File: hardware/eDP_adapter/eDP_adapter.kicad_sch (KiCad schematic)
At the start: 90 parts, among them J1 DF12NB(3.0)-30DS-0.5V(51), J2 DF12NB(3.0)-30DS-0.5V(51), J3 Conn_01x40, J4 Barrel_Jack_MountingPin, Q1 2N7002WT1G, U1 NCS8801, U2 EA3036A, U3 MT3608

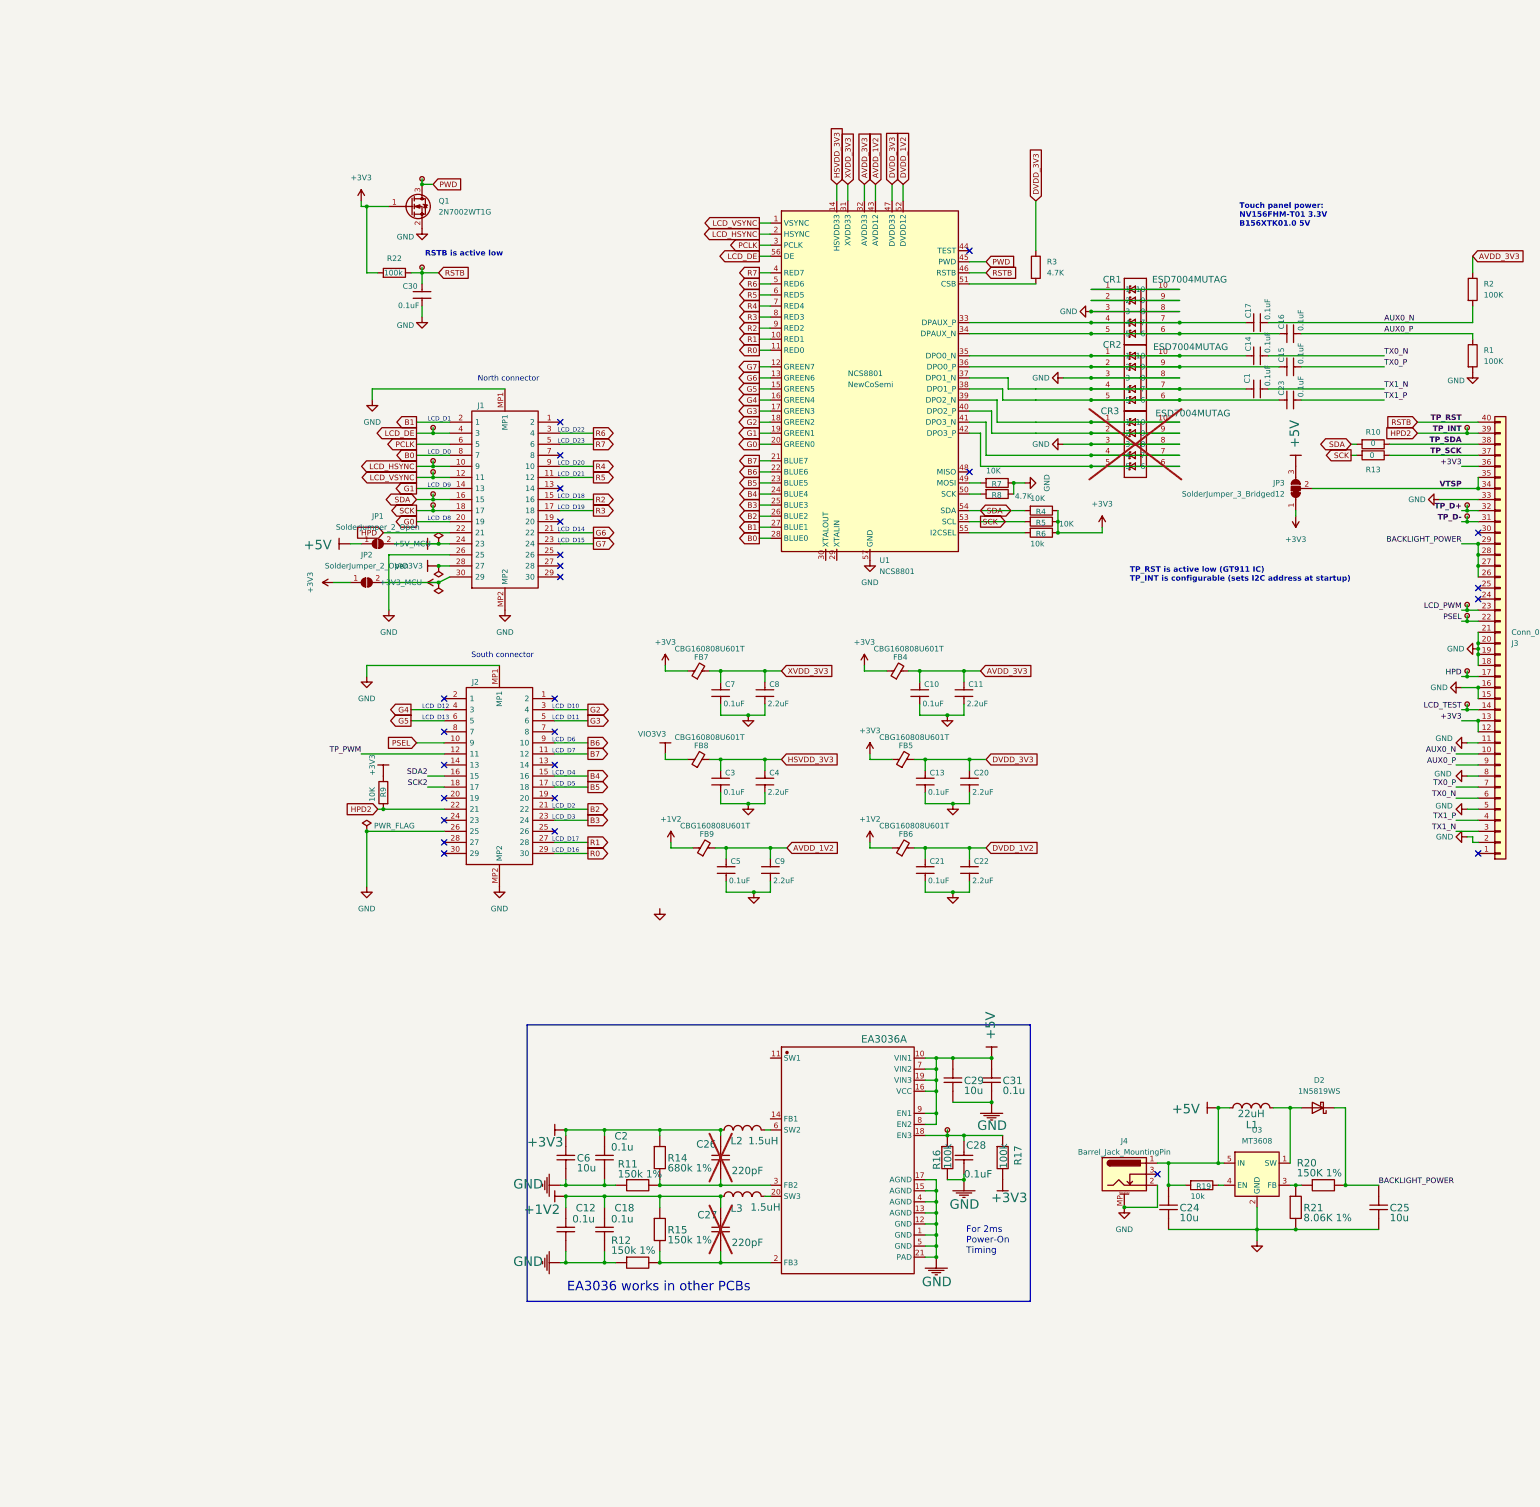
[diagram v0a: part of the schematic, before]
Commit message: make eDP adaoter 4 layer and misc fixes (like missing crystal)
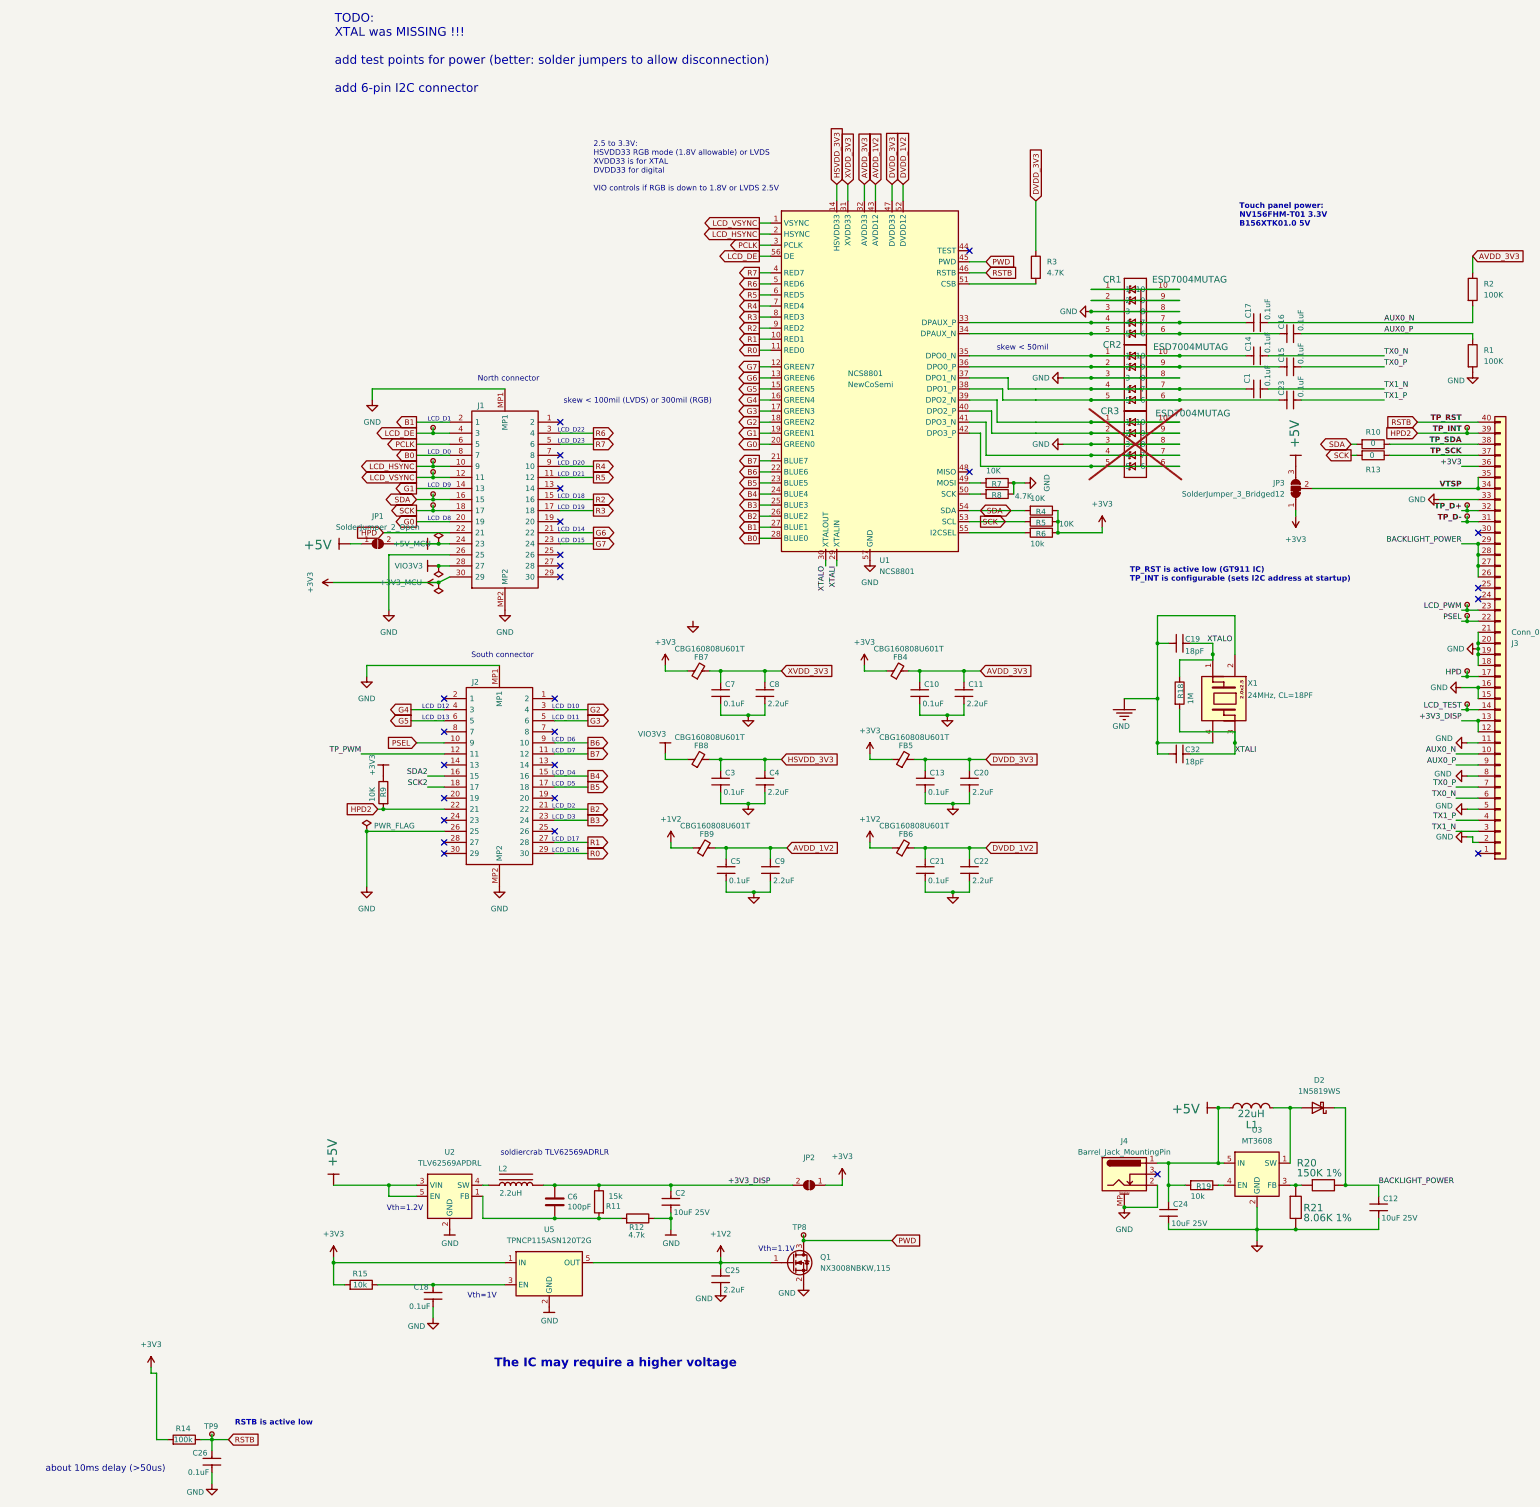
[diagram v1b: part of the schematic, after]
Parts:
- removed C12, C18, C2: 0.1u, Capacitor_SMD:C_0603_1608Metric, symbol C_0402_US_4
- removed C24, C25, C29, C6: 10u, Capacitor_SMD:C_0603_1608Metric, symbol C_0402_US_7
- removed C26, C27: 220pF, Capacitor_SMD:C_0603_1608Metric, symbol C_0402_US_4
- removed C28: 0.1uF, Capacitor_SMD:C_0402_1005Metric, symbol GRM188B30J106ME47D_14
- removed C30: 0.1uF, Library:C_0402_1005Metric, symbol Periph-altium-import:0_CAP
- removed C31: 0.1u, Capacitor_SMD:C_0603_1608Metric, symbol C_0402_US_6
- removed L2: 1.5uH, Inductor_SMD:L_Cenker_CKCS201610, symbol CKCS201610-2.2UH/M-N_1
- removed L3: 1.5uH, Inductor_SMD:L_Cenker_CKCS201610, symbol CKCS201610-2.2UH/M-N
- removed R11: 150k 1%, Resistor_SMD:R_0402_1005Metric, symbol R_0402_EU_2
- removed R12: 150k 1%, Resistor_SMD:R_0402_1005Metric, symbol R_0402_EU
- removed R14: 680k 1%, Resistor_SMD:R_0402_1005Metric, symbol R_0402_EU_3
- removed R15: 150k 1%, Resistor_SMD:R_0402_1005Metric, symbol R_0402_EU_1
- removed R16: 100k, Resistor_SMD:R_0402_1005Metric, symbol R_0603_EU_1
- removed R17: 100k, Resistor_SMD:R_0402_1005Metric, symbol R_0603_EU
- removed R22: 100k, Resistor_SMD:R_0402_1005Metric, symbol Device:R
- removed TP10, TP11: TestPoint_Small, TestPoint:TestPoint_Pad_D1.0mm, symbol Connector:TestPoint_Small
- removed U2: EA3036A, Package_DFN_QFN:WQFN-20-1EP_3x3mm_P0.4mm_EP1.7x1.7mm, symbol EA3036A
- added C12, C2, C24: 10uF 25V, Capacitor_SMD:C_0805_2012Metric, symbol Periph-altium-import:0_CAP
- added C18, C26: 0.1uF, Library:C_0402_1005Metric, symbol Periph-altium-import:0_CAP
- added C19, C32: 18pF, Library:C_0402_1005Metric, symbol D1s-altium-import:1_mirrored_CAP
- added C25: 2.2uF, Library:C_0402_1005Metric, symbol Periph-altium-import:0_CAP
- added C6: 100pF, Capacitor_SMD:C_0201_0603Metric, symbol Device:C
- added L2: 2.2uH, Library:Murata_DFE201612P-2R2M=P2, symbol Periph-altium-import:0_L
- added R11: 15k, Resistor_SMD:R_0201_0603Metric, symbol Device:R
- added R12: 4.7k, Resistor_SMD:R_0201_0603Metric, symbol Device:R
- added R14: 100k, Resistor_SMD:R_0402_1005Metric, symbol Device:R
- added R15: 10k, Resistor_SMD:R_0402_1005Metric, symbol Device:R
- added R18: 1M, Resistor_SMD:R_0402_1005Metric, symbol Device:R
- added TP8: TestPoint_Small, TestPoint:TestPoint_Pad_D1.0mm, symbol Connector:TestPoint_Small
- added U2: TLV62569APDRL, Package_TO_SOT_SMD:SOT-563, symbol Regulator_Switching:TLV62569DRL
- added U5: TPNCP115ASN120T2G, Package_TO_SOT_SMD:SOT-23-5, symbol Regulator_Linear:NCP115AMX250TCG
- added X1: 24MHz, CL=18PF, Library:Crystal_SMD_2520-4Pin_2.5x2.0mm, symbol D1s-altium-import:3_mirrored_XTAL3225
- Q1: value 2N7002WT1G -> NX3008NBKW,115; MPN 2N7002WT1G -> NX3008NBKW,115
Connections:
- net +1V2: now also Q1.1 (G), C25.1, U5.5 (OUT)
- net +3V3: now also J1.30 (29), R14.2, R15.2, U5.1 (IN); no longer J3.12 (Pin_12), J3.13 (Pin_13), Q1.1 (G)
- net +5V: now also C24.1, U2.3 (VIN), U2.5 (EN)
- net BACKLIGHT_POWER: now also C12.1
- net GND: now also C12.2, C18.2, C19.2, C2.2, C24.2, C25.2, C26.2, C32.2, R12.1, U2.2 (GND), U5.2 (GND), U5.5 (OUT), X1.2 (NC1), X1.4 (NC2)
- net PWD: now also TP8.1
- net RSTB: now also C26.1, R14.1
- net XTALI: now reaches U1.29 (XTALIN)
- net XTALI: now also C32.1, R18.2, X1.3 (X2)
- net XTALO: now reaches U1.30 (XTALOUT)
- net XTALO: now also C19.1, R18.1, X1.1 (X1)
- net +3V3_MCU renamed +3V3_DISP
- net +3V3_DISP: now also J3.12 (Pin_12), J3.13 (Pin_13), C2.1, C6.2, L2.1, R11.1; no longer J1.30 (29)
- new net: C6.1, R11.2, R12.2, U2.1 (FB)
- new net: L2.2, U2.4 (SW)
- new net: C18.1, R15.1, U5.3 (EN)
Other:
- note added: "2.5 to 3.3V: HSVDD33 RGB mode (1.8V allowable) or LVDS XVDD33 is for XTAL DVDD33 for digital VIO controls if RGB is down to 1.8V or LVDS 2.5V"
- note added: "TODO: XTAL was MISSING !!! add test points for power (better: solder jumpers to allow disconnection) add 6-pin I2C connector"
- note added: "The IC may require a higher voltage"
- note added: "Vth=1.1V"
- note added: "Vth=1.2V"
- note added: "Vth=1V"
- note added: "about 10ms delay (>50us)"
- note added: "skew < 100mil (LVDS) or 300mil (RGB)"
- note added: "skew < 50mil"
- note added: "soldiercrab TLV62569ADRLR"
- note removed: "EA3036 works in other PCBs"
- note removed: "For 2ms Power-On Timing"
- company: Copyright (C) 2025 Victor Suarez Rovere -> Copyright (C) 2025-2026 Victor Suarez Rovere

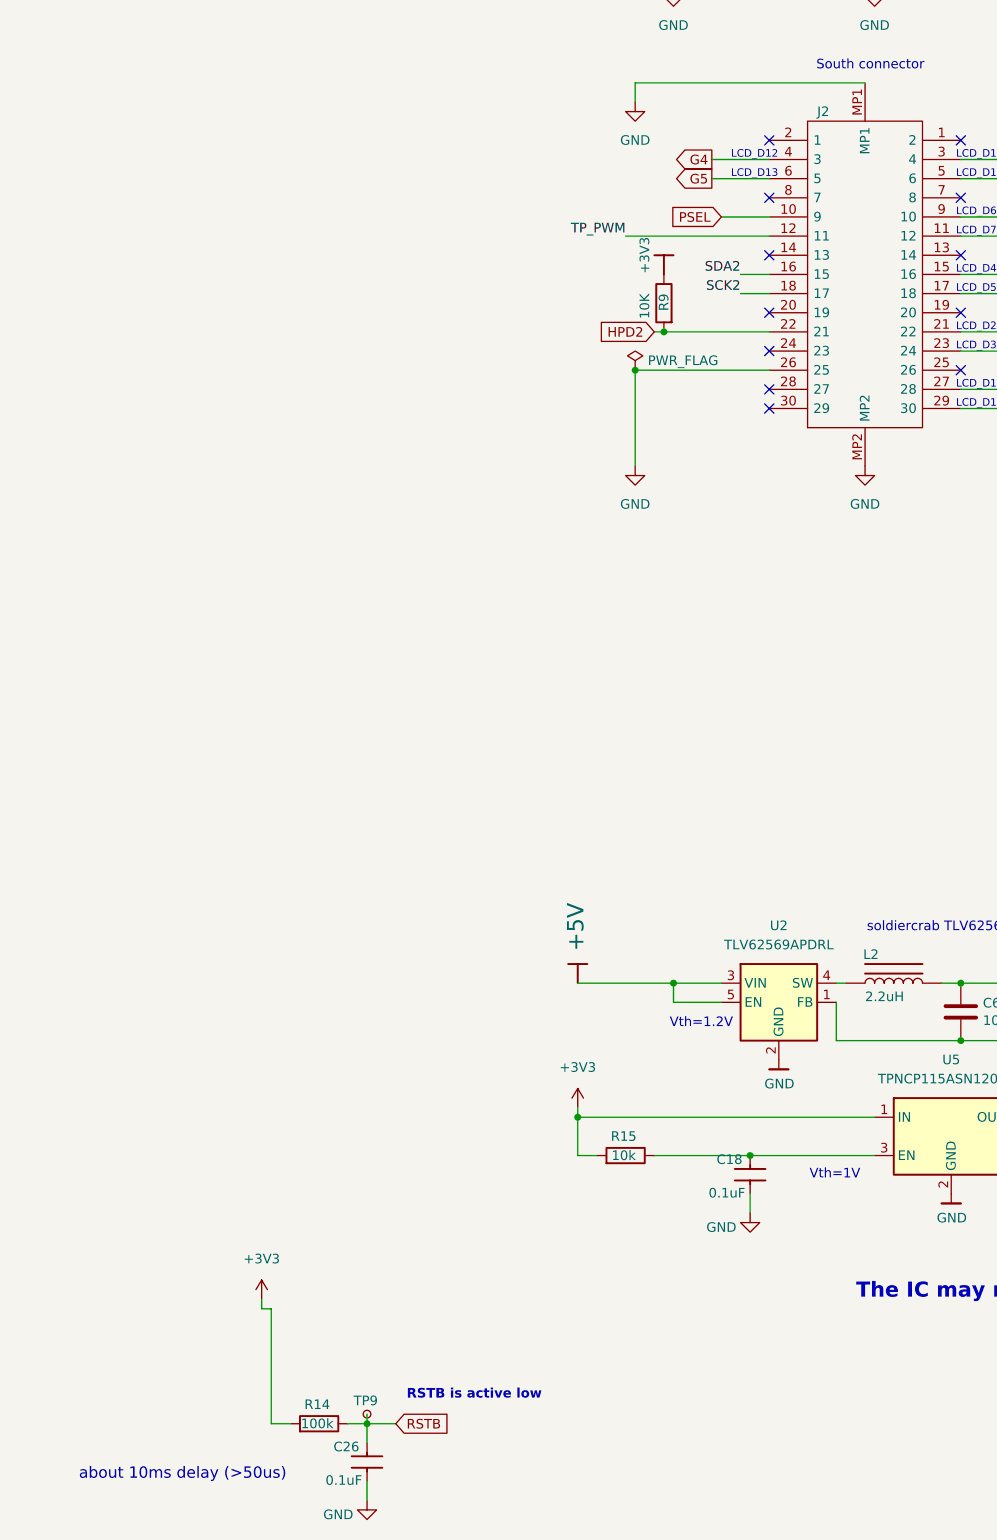
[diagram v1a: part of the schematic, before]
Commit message: fixed mixup of pins G5/G4 (3rd diff pair ODD) and DE/PCLK (3rd diff pair EVEN), now with correct polarity for diff pairs
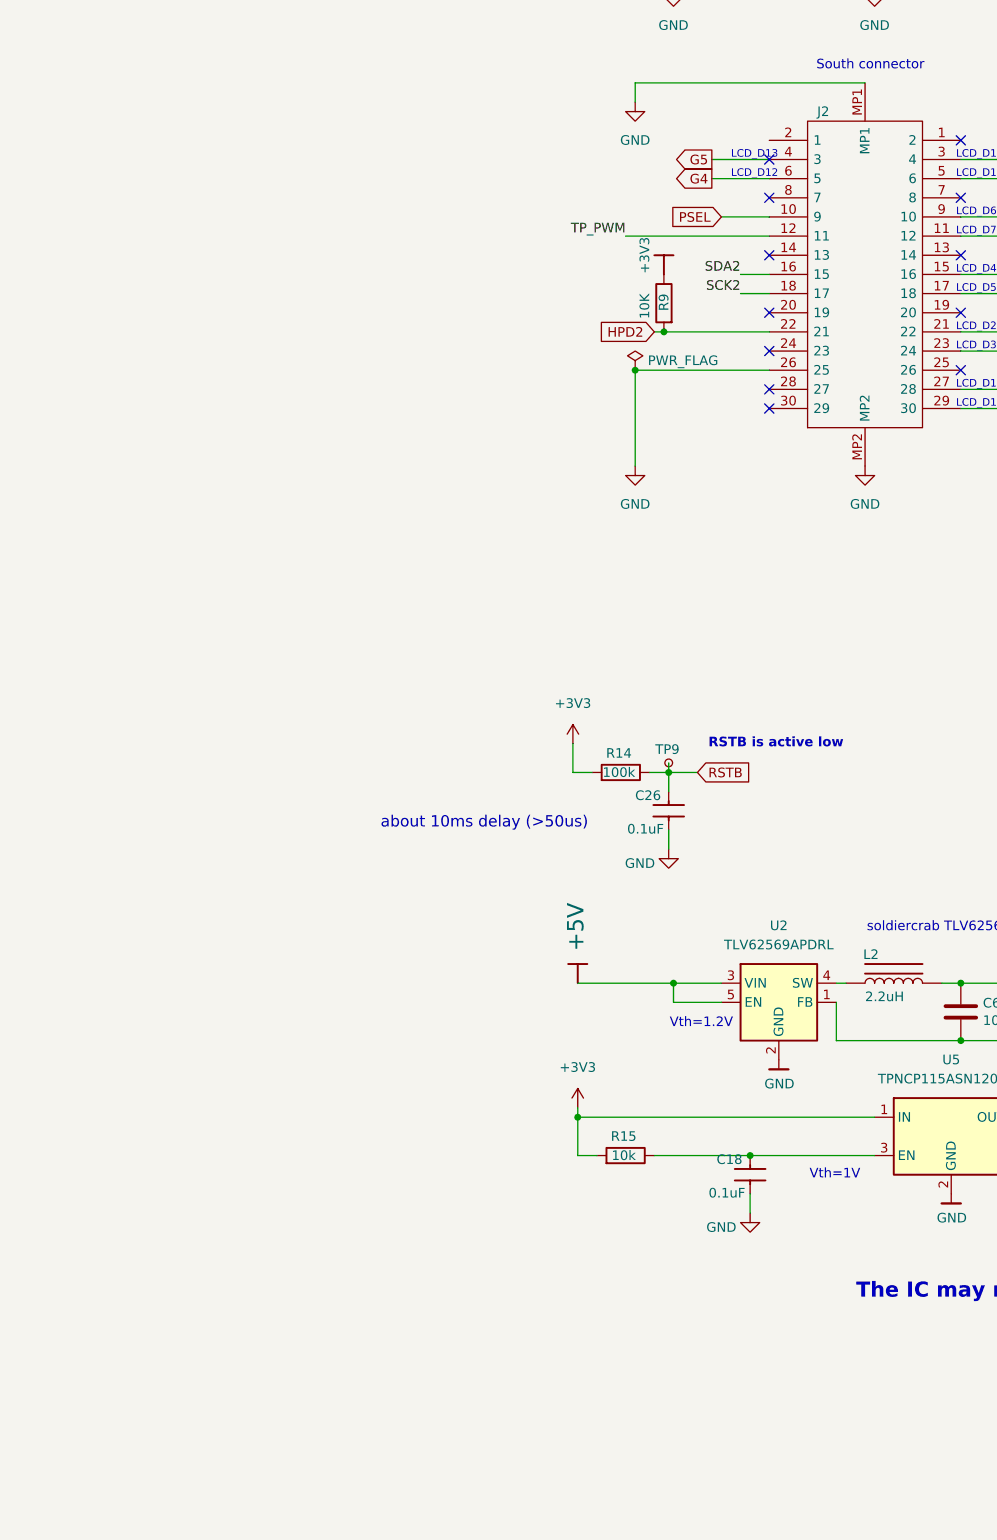
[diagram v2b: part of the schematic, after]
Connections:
- net G4: now also J2.6 (5); no longer J2.4 (3)
- net G5: now also J2.4 (3); no longer J2.6 (5)
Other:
- moved on the sheet: C26, R14, TP9
